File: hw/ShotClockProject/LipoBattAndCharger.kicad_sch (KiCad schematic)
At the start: 28 parts, among them IC1 TP4056-42-ESOP8_Rearanged, J4 SM03B-SRSS-TB(LF)(SN)(P), J5 Conn_01x02_Pin, J6 Conn_01x03_Pin, Q1 Q_PMOS_SGD, Q3 Q_NPN_BCE, Q4 Q_NPN_BCE

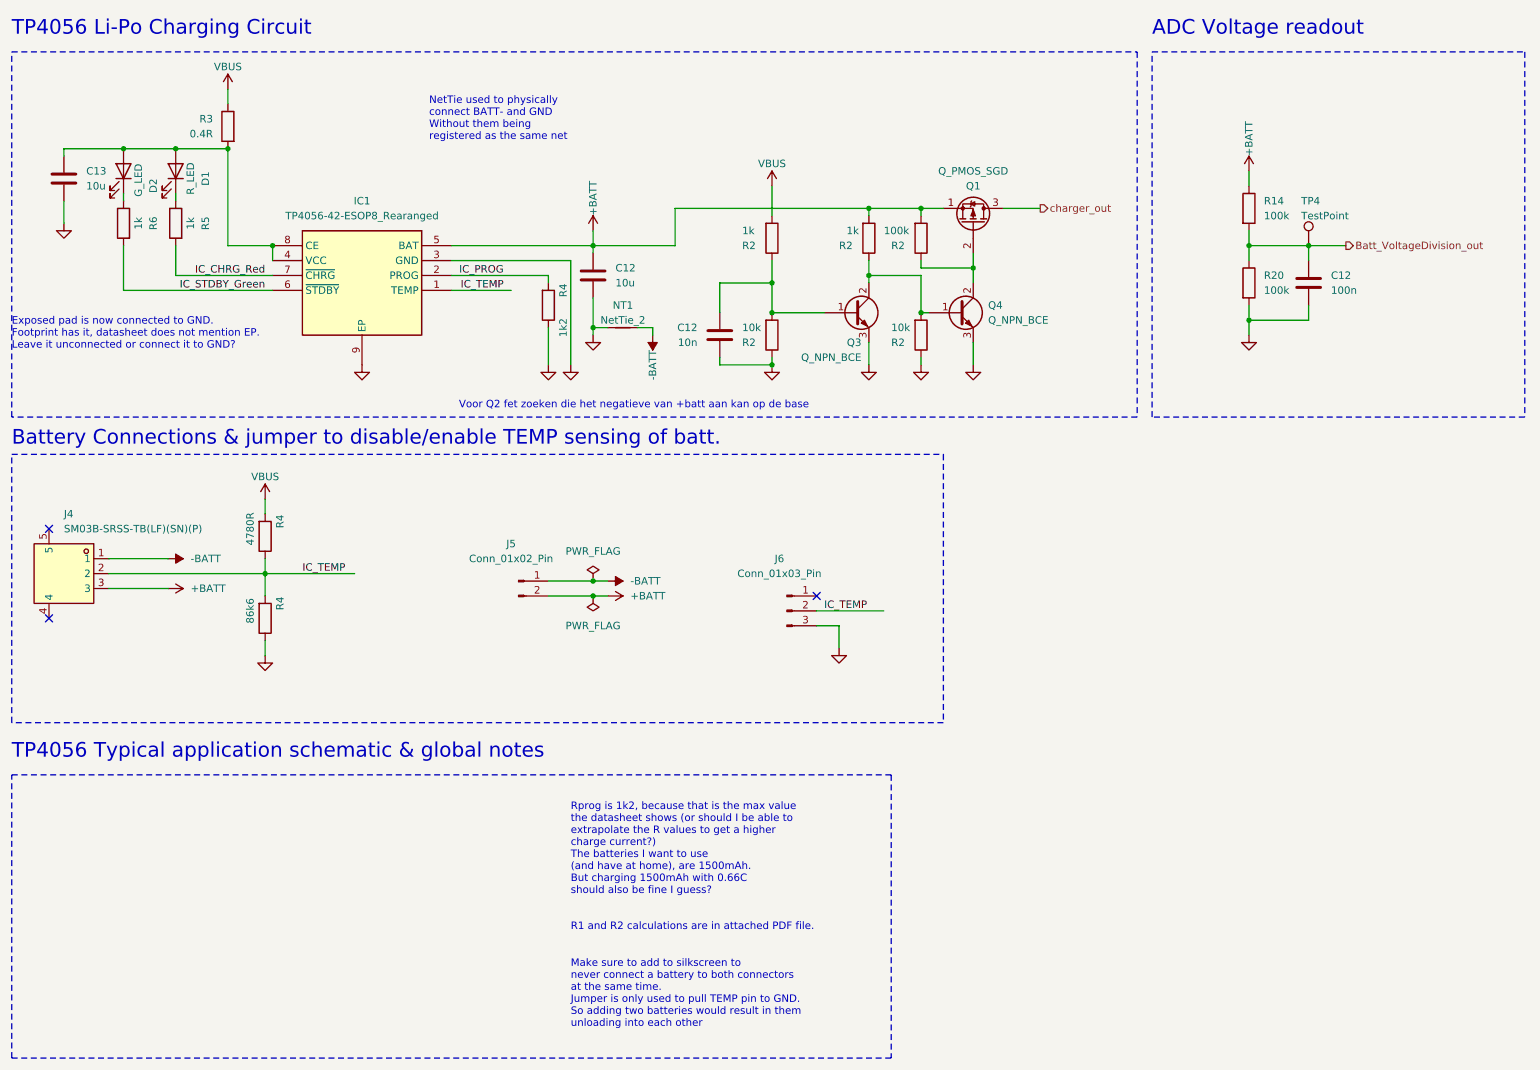
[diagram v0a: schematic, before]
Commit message: Added I2C support
Calculated pull-up resistor values
Added 6 pin female headers to mainboard
Added nRESET line for the I2C chips
Removed PCB routing and part placement
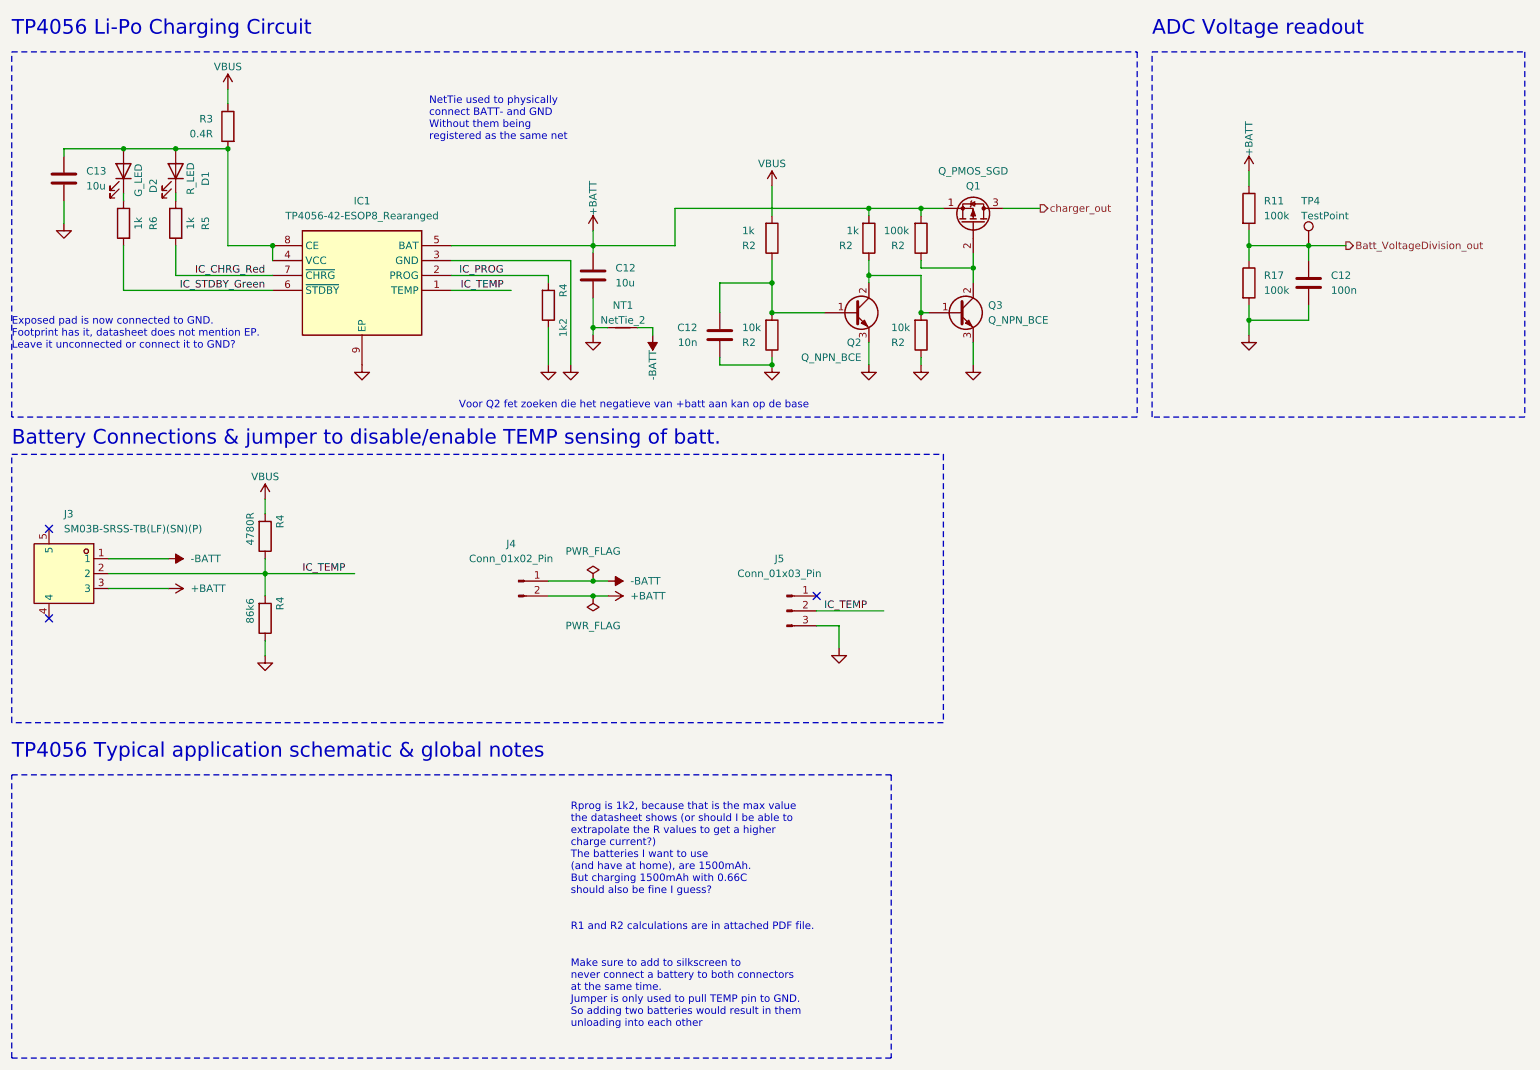
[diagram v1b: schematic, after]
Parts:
- renumbered J4 to J3, J5 to J4, J6 to J5, Q3 to Q2, Q4 to Q3, R14 to R11, R20 to R17

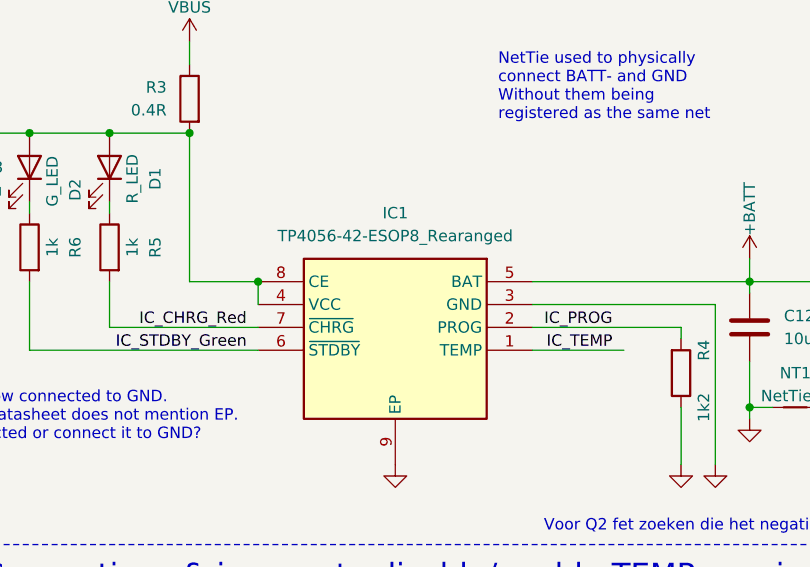
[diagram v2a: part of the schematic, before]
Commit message: Routed V regulators on mainboard
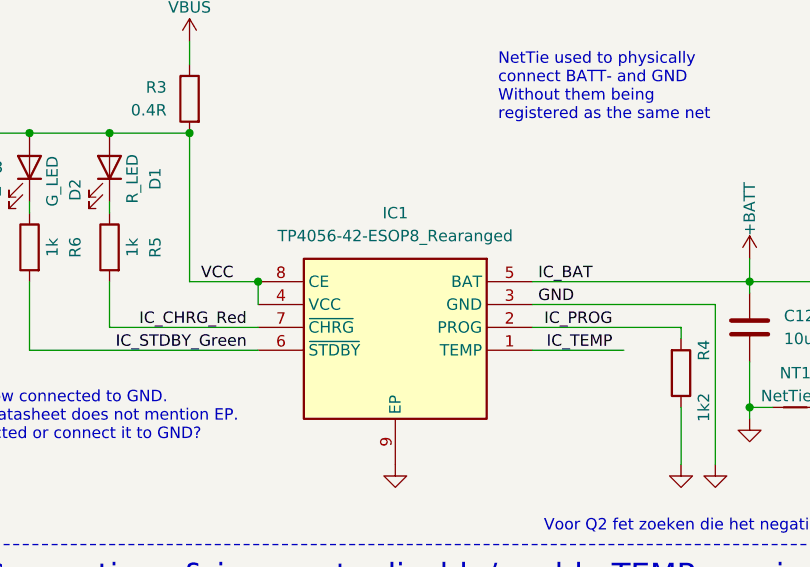
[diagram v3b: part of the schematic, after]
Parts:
- C12, C13: footprint Capacitor_SMD:C_0603_1608Metric -> Capacitor_SMD:C_0402_1005Metric
- IC1: footprint Package_SO:Texas_HSOP-8-1EP_3.9x4.9mm_P1.27mm_ThermalVias -> Package_SO:Texas_HSOP-8-1EP_3.9x4.9mm_P1.27mm
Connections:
- net VCC: now reaches C13.1, D1.2 (A), D2.2 (A), IC1.4 (VCC), IC1.8 (CE), R3.2
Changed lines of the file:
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@@
+    (effects (font (size 1.27 1.27)) (justify left bottom))
+  )
+  (label "VCC" (at 60.96 55.88 0) (fields_autoplaced)
     (effects (font (size 1.27 1.27)) (justify left bottom))
   )
@@
     (effects (font (size 1.27 1.27)) (justify right bottom))
   )
+  (label "IC_BAT" (at 98.425 55.88 0) (fields_autoplaced)
+    (effects (font (size 1.27 1.27)) (justify left bottom))
+  )
   (label "IC_TEMP" (at 161.29 118.11 0) (fields_autoplaced)
     (effects (font (size 1.27 1.27)) (justify left bottom))
@@
   (label "IC_TEMP" (at 106.68 63.5 180) (fields_autoplaced)
     (effects (font (size 1.27 1.27)) (justify right bottom))
+  )
+  (label "GND" (at 98.425 58.42 0) (fields_autoplaced)
+    (effects (font (size 1.27 1.27)) (justify left bottom))
   )
   (hierarchical_label "charger_out" (shape output) (at 198.12 49.53 0) (fields_autoplaced)
@@
       (effects (font (size 1.27 1.27)) (justify left))
     )
-    (property "Footprint" "Capacitor_SMD:C_0603_1608Metric" (at 122.8852 64.77 0)
+    (property "Footprint" "Capacitor_SMD:C_0402_1005Metric" (at 122.8852 64.77 0)
       (effects (font (size 1.27 1.27)) hide)
     )
@@
       (effects (font (size 1.27 1.27)) (justify left))
     )
-    (property "Footprint" "Capacitor_SMD:C_0603_1608Metric" (at 142.5448 74.93 0)
+    (property "Footprint" "Capacitor_SMD:C_0402_1005Metric" (at 142.5448 74.93 0)
       (effects (font (size 1.27 1.27)) hide)
     )
@@
       (effects (font (size 1.27 1.27)))
     )
-    (property "Footprint" "Package_SO:Texas_HSOP-8-1EP_3.9x4.9mm_P1.27mm_ThermalVias" (at 71.12 150.8 0)
+    (property "Footprint" "Package_SO:Texas_HSOP-8-1EP_3.9x4.9mm_P1.27mm" (at 71.12 150.8 0)
       (effects (font (size 1.27 1.27)) (justify left top) hide)
     )
@@
       (effects (font (size 1.27 1.27)) (justify right))
     )
-    (property "Footprint" "Capacitor_SMD:C_0603_1608Metric" (at 30.7848 48.26 0)
-      (effects (font (size 1.27 1.27)) hide)
-    )
+    (property "Footprint" "Capacitor_SMD:C_0402_1005Metric" (at 30.7848 48.26 0)
+      (effects (font (size 1.27 1.27)) hide)
+    )

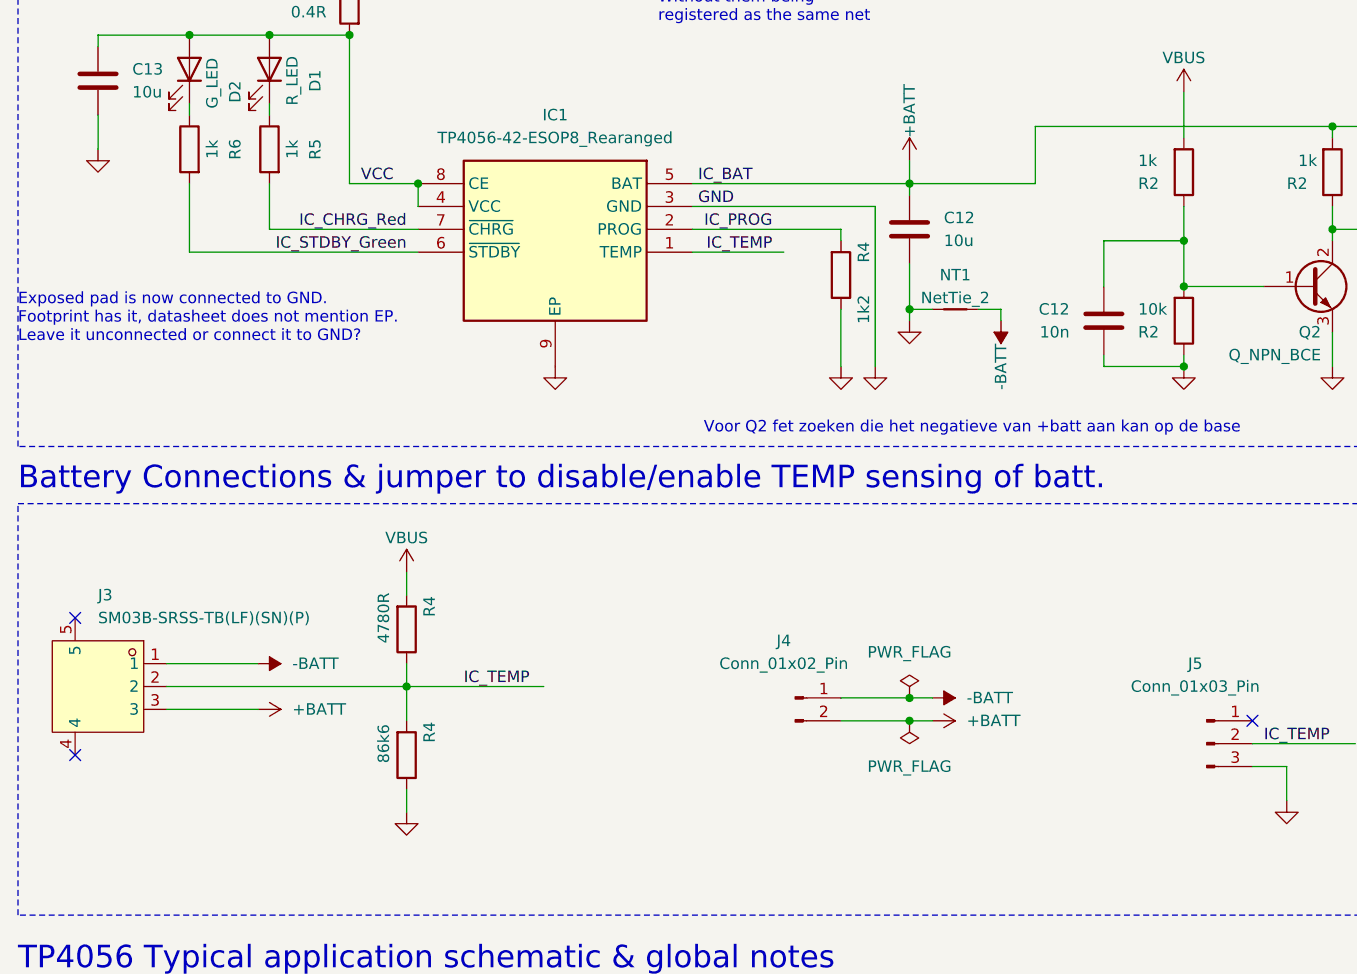
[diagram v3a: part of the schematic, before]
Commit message: Routing on mainboard for LiPo charger
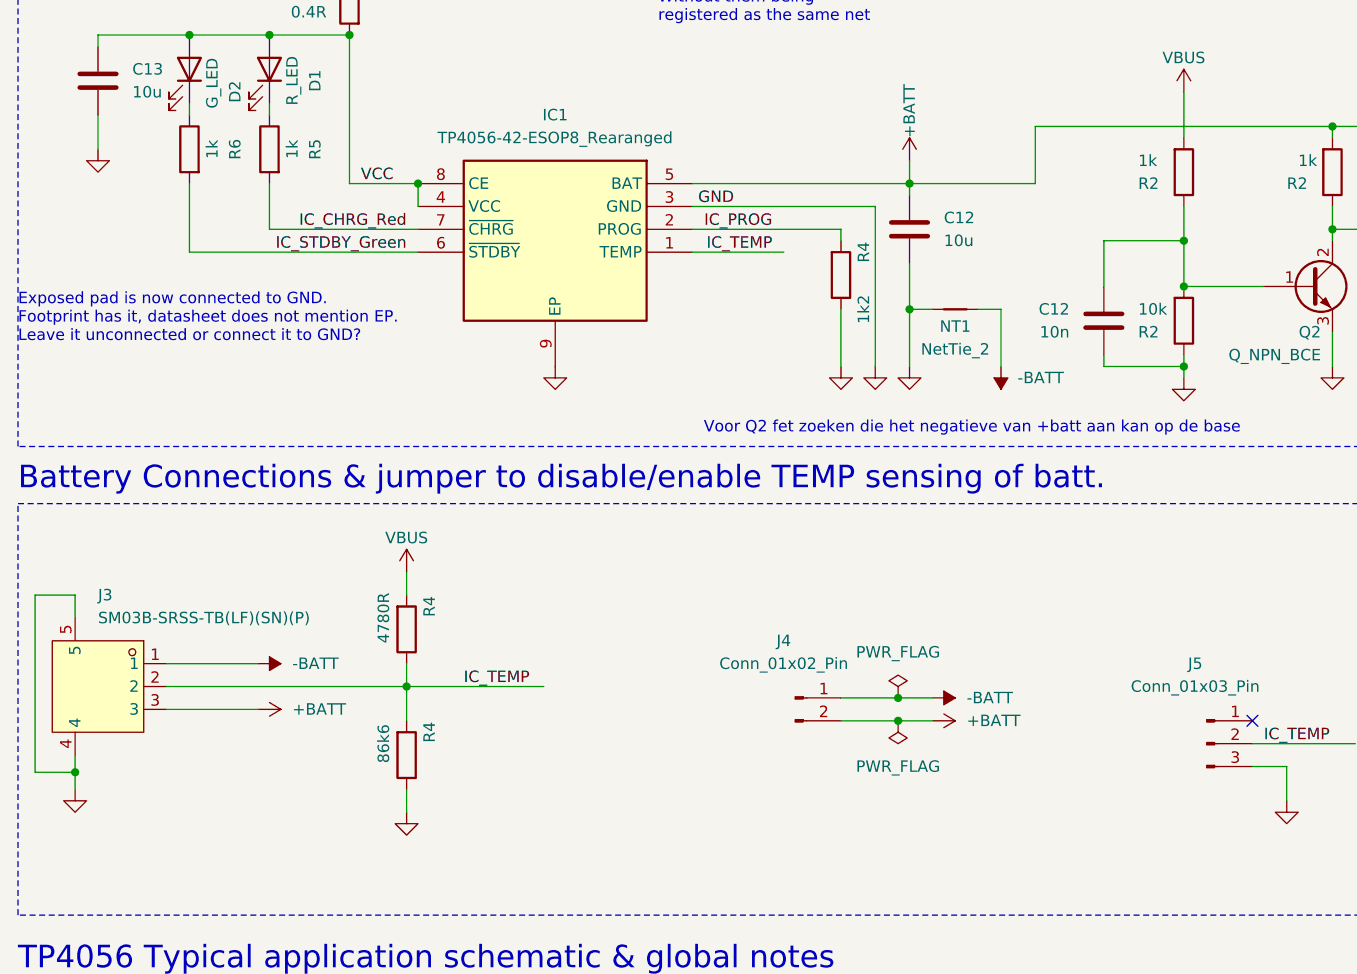
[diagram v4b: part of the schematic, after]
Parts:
- NT1: footprint NetTie:NetTie-2_SMD_Pad2.0mm -> NetTie:NetTie-2_SMD_Pad0.5mm
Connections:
- net GND: now also J3.4, J3.5
- no-connect marks 3 -> 1
